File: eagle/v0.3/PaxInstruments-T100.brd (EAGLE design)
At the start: 46 x 17.1 mm, 32 parts, among them U1 Attiny85

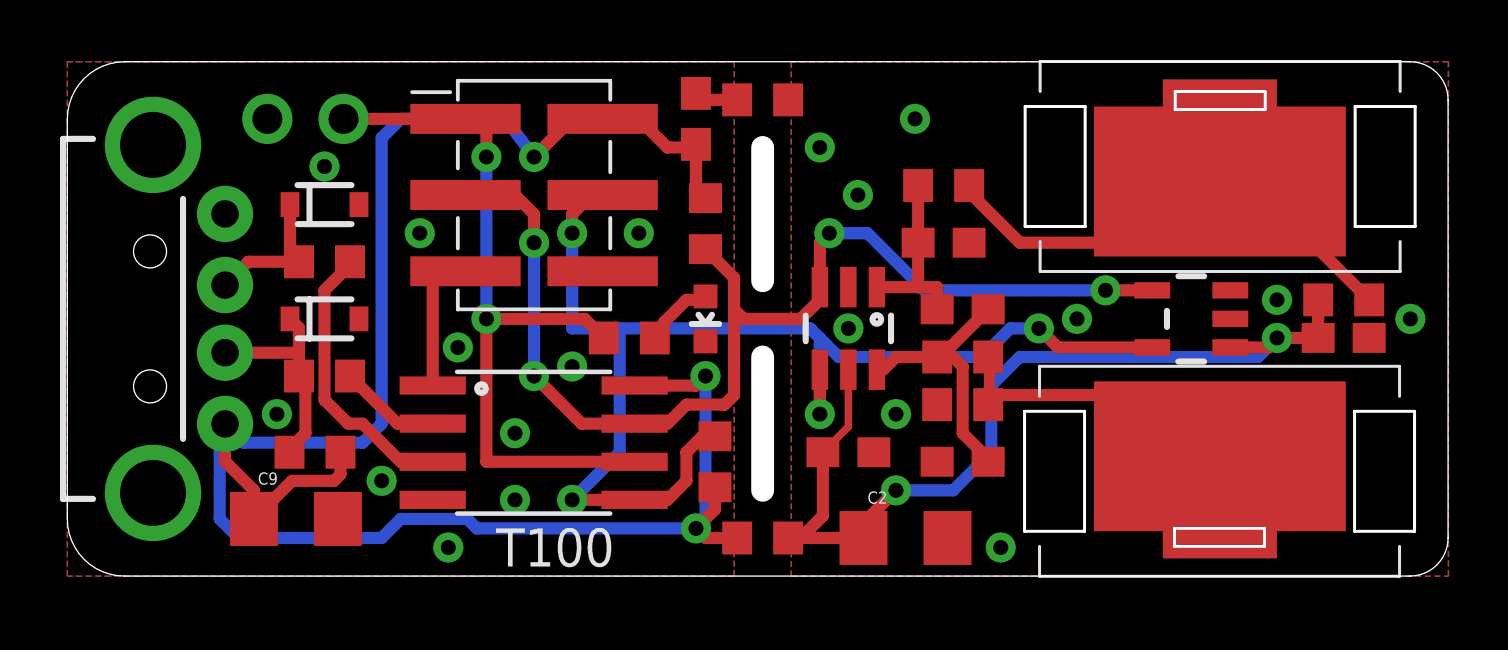
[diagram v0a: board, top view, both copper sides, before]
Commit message: Made via holes smaller. Verified design. Ready to order PCBs. Added 0.3 fab files.
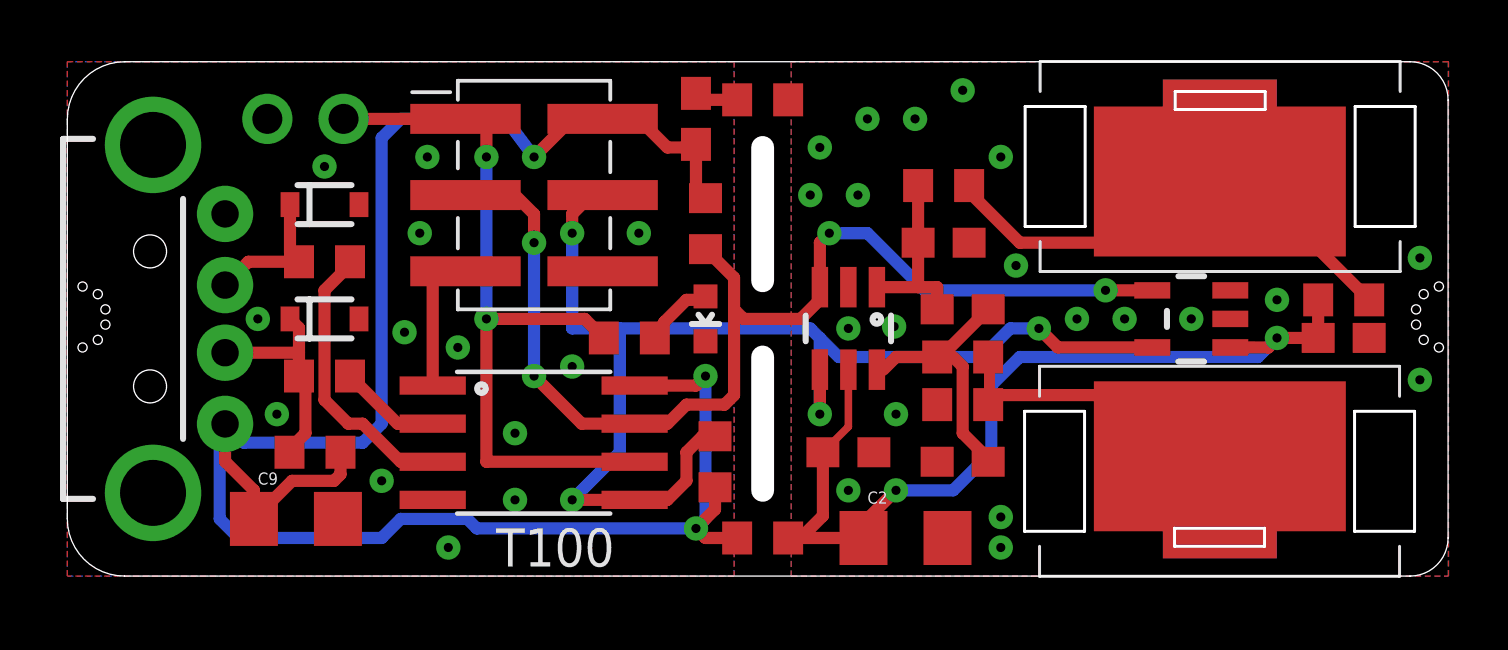
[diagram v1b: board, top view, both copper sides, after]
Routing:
- net GND: vias 10 -> 13
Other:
- board text added: "Mount to panel here"

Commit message: Changed USB connector. Updated thermocouple footprint. Rerouted board.
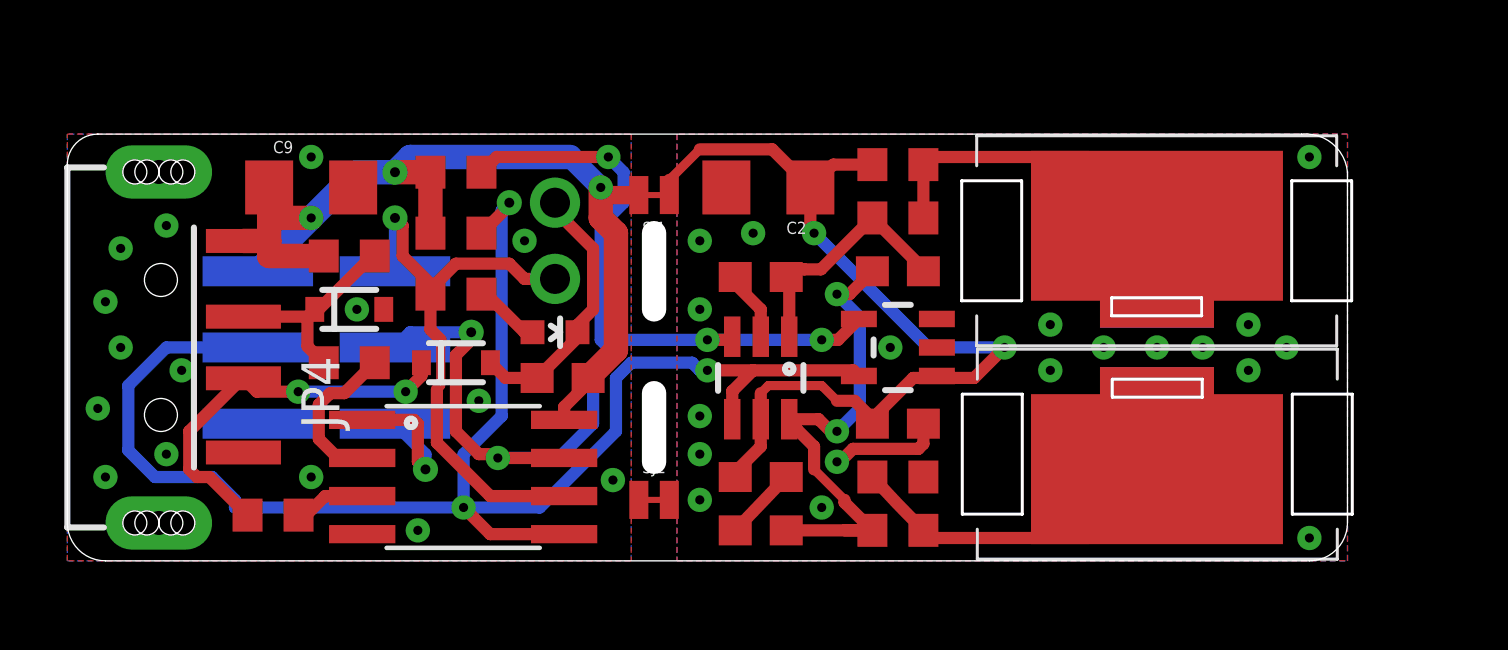
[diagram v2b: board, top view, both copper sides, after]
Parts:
- removed JP1: USB-A-H, SparkFun-Connectors:USB-A-H
- removed R11, R12: 0R, rcl:R0603
- added JP4: USBA-SMD-MALE, SparkFun-Connectors:USB-A-SMT-MALE
- added SJ1, SJ2: JUMPER-PAD-2-NC_BY_TRACENO_SILK, SparkFun-Passives:PAD-JUMPER-2-NC_BY_TRACE_NO_SILK
- moved R4 15.5 mm to (27.7, 13.7)
- moved C5 15.1 mm to (27.7, 5.08)
- moved C2 12.5 mm to (23.4, 13.0), turned to 180 degrees
- moved R7 11.5 mm to (13.0, 11.4), turned to 180 degrees
- moved C9 11.1 mm to (8.13, 13.0)
- moved U$4 9.83 mm to (27.7, 7.62)
- moved C1 9.71 mm to (16.5, 6.60), turned to 180 degrees
- moved JP3 9.26 mm to (16.3, 11.2), turned to 270 degrees
- moved R1 8.62 mm to (6.86, 2.03)
- moved JP2 8.59 mm to (8.64, 7.62), flipped to the bottom
- moved R8 8.49 mm to (13.0, 13.5), turned to 180 degrees
- moved C6 7.11 mm to (23.1, 1.52)
- moved D1 6.85 mm to (13.0, 7.11)
- moved R9 6.64 mm to (9.40, 10.7), turned to 180 degrees
- moved C7 6.20 mm to (23.1, 9.97), turned to 180 degrees
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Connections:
- net AGND: now also SJ2.2; no longer R11.1
- net A_5V: now also SJ1.1; no longer R12.1
- net GND: now also JP4.VBUS1, SJ2.1; no longer JP1.GND, R11.2
- net N$1: now also JP4.D+1; no longer JP1.D-
- net N$2: now also JP4.D-1; no longer JP1.D+
- net USB_5V: now also JP4.GND1, SJ1.2; no longer JP1.VBUS, R12.2
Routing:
- net USB_5V: track 68.5 -> 33.2 mm
- net SDA: track 42.1 -> 53.3 mm, vias 4 -> 3
- net AGND: track 0.00 -> 8.96 mm, vias 20 -> 19
- net N$2: track 4.82 -> 13.2 mm, vias 0 -> 2
- net TC-: track 9.03 -> 17.3 mm, vias 0 -> 2
- net GND: track 1.46 -> 8.91 mm, vias 13 -> 15
- net D+: track 9.42 -> 2.38 mm
- net N$4: track 16.6 -> 10.6 mm
- net SPARE: track 25.3 -> 19.8 mm, vias 2 -> 1
- net TC+: track 6.14 -> 8.59 mm
- net D-: track 3.41 -> 5.30 mm
- net N$3: track 13.1 -> 11.3 mm
- net /RST: track 4.78 -> 5.48 mm, vias 0 -> 1
- net A_5V: track 31.7 -> 31.1 mm
- net SCL: track 38.1 -> 37.7 mm, vias 4 -> 5
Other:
- board size 46 x 17.1 mm -> 42.7 x 14.2 mm
- board text added: "Keep edge clean"
- board text added: "Pax Instruments Temperature LabStick T100 v0.3"
- board text removed: "Mount to panel here"
- board text removed: "Pax Instruments Temperature LabStick T100 v0.3 beta"
- board text removed: "T100"
